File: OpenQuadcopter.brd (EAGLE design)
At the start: 100 x 100 mm, 78 parts, among them U1 MPU-6000QFN-24

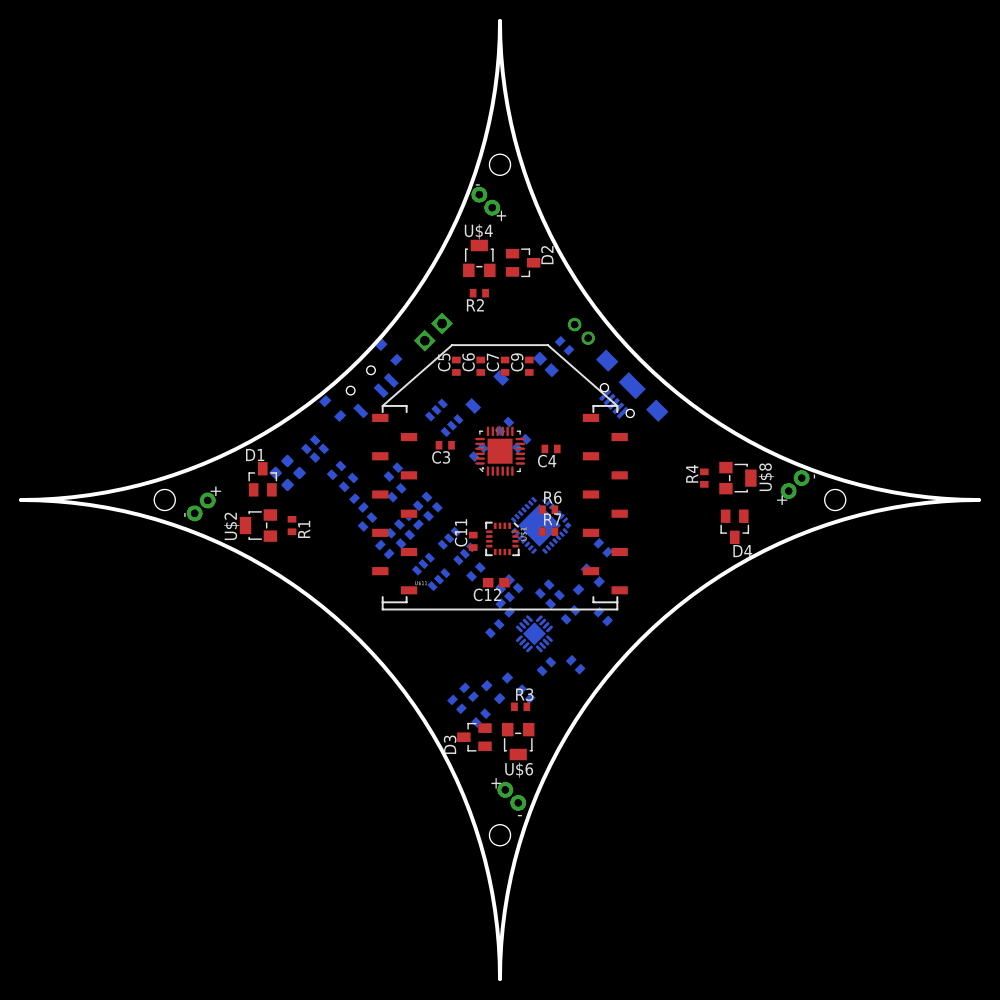
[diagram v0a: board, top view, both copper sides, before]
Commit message: smooth the corner of quadcopter.
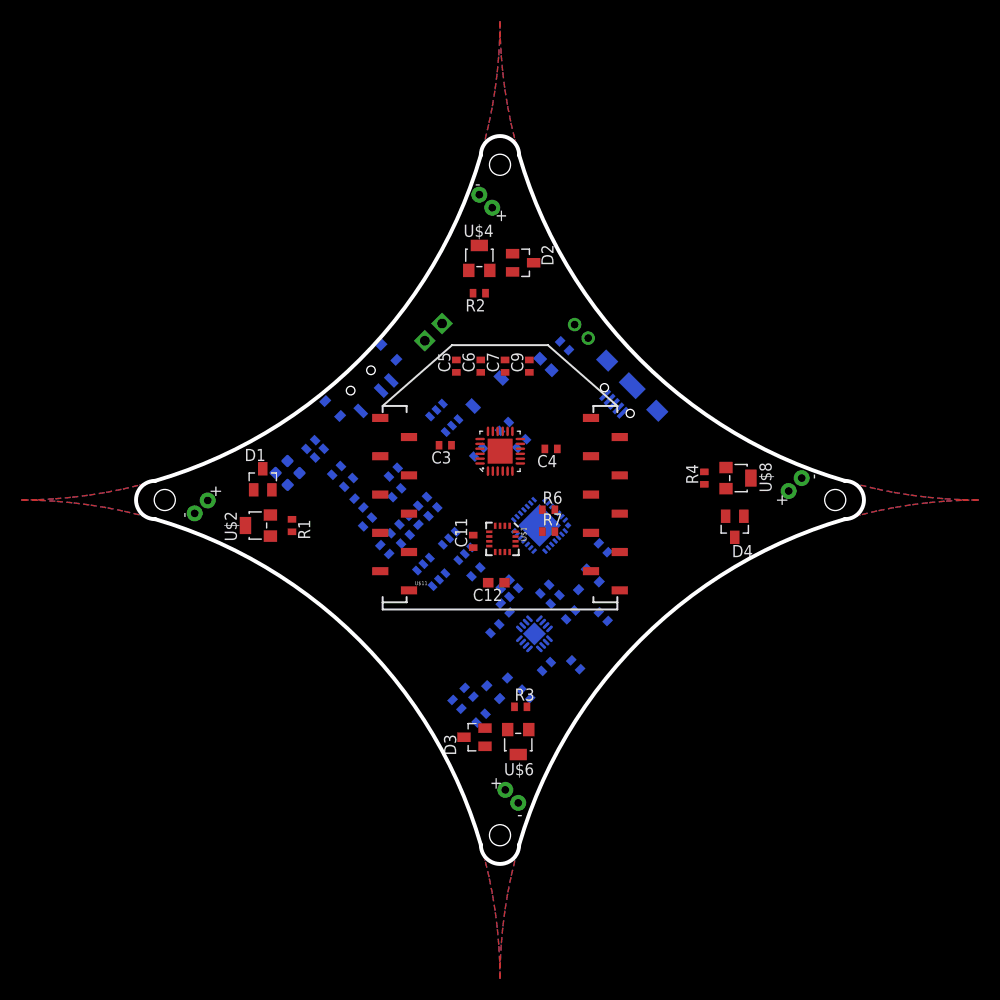
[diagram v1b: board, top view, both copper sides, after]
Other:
- board size 100 x 100 mm -> 76 x 76 mm

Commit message: Publish openquadcopter extention board.
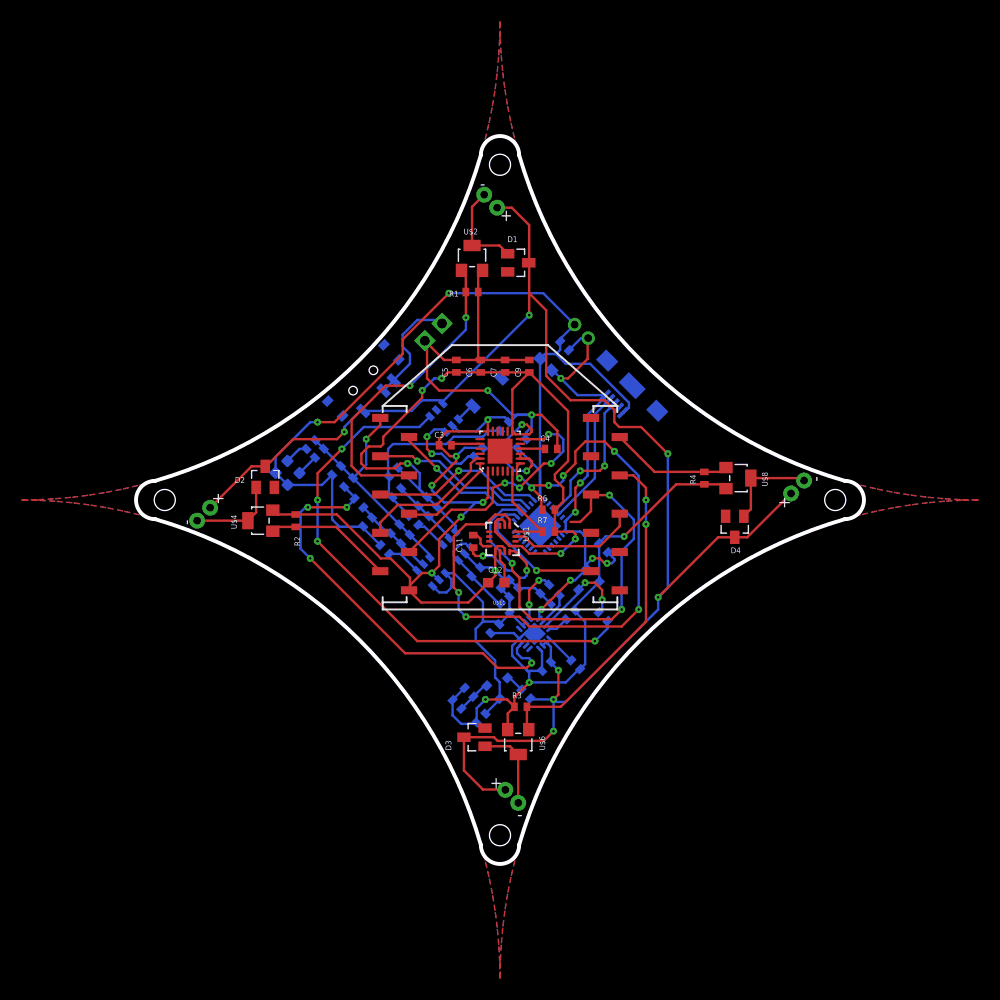
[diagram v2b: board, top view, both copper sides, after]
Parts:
- moved U$3 49.0 mm to (4.70, 34.4), turned to 0 degrees
- moved U$5 48.8 mm to (-34.2, 4.19), turned to 90 degrees
- moved U$2 35.8 mm to (-2.92, 25.3), turned to 0 degrees
- moved U$4 35.7 mm to (-25.0, -2.16), turned to 90 degrees
- moved D2 35.0 mm to (-24.5, 2.41), turned to 0 degrees
- moved D1 35.0 mm to (1.91, 24.8), turned to 270 degrees
- moved R1 30.8 mm to (-2.92, 21.7), turned to 180 degrees
- moved R2 30.5 mm to (-21.3, -2.16), turned to 270 degrees
- moved U$9 0.36 mm to (34.3, -4.32)
- moved U$12 0.25 mm to (-14.3, 12.5)
- moved U$14 0.09 mm to (4.18, -2.73), turned to 315 degrees
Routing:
- net GND: track 0.00 -> 210.9 mm, vias 0 -> 12
- net BAT: track 0.00 -> 164.2 mm, vias 0 -> 7
- net VCCA: track 0.00 -> 97.7 mm, vias 0 -> 7
- net DGND: track 0.00 -> 97.5 mm, vias 0 -> 2
- net N$4: track 0.00 -> 71.7 mm, vias 0 -> 8
- net N$15: track 0.00 -> 57.2 mm, vias 0 -> 4
- net VBUS: track 0.00 -> 49.4 mm, vias 0 -> 7
- net BOOT0: track 0.00 -> 45.5 mm, vias 0 -> 3
- net /PGOOD: track 0.00 -> 44.8 mm, vias 0 -> 4
- net MOTOR/PA6: track 0.00 -> 35.8 mm, vias 0 -> 2
- net MOTOR/PC8: track 0.00 -> 33.4 mm, vias 0 -> 2
- net VCOM: track 0.00 -> 31.8 mm
- net INT/PA4: track 0.00 -> 27.8 mm, vias 0 -> 4
- net VCCD: track 0.00 -> 24.7 mm, vias 0 -> 1
- net AGND: track 0.00 -> 20.4 mm
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
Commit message: Fixed.
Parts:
- C10, C18, C22, C23: value (none) -> 100nF
- C13, C14, C16, C21: value (none) -> 4.7uF; device openmotestm:C0402 -> openmotestm:C0603
- C15, C20: value (none) -> 15pF
- C17, C19: value (none) -> 10nF
- C24: value (none) -> 1uF
- C8: value (none) -> 10uF; device openmotestm:C0402 -> openmotestm:C0603
- R1, R11, R2, R21, R22, R24, R25, R3, R4, R9: value (none) -> 10K
- R10, R8: value (none) -> 1.2K
- R12: value (none) -> 10R
- R13: value (none) -> 39K
- R14, R16: value (none) -> 30K
- R15: value (none) -> 42.2K
- R17: value (none) -> 150K
- R18: value (none) -> 300K
- R19, R20: value (none) -> 1K
- R23: value (none) -> 100K
- R26: value (none) -> 20K
- R27, R28: value (none) -> 0R
- U$1: value HMC5883LSMD -> HMC5883L-SMD
- U$2, U$4, U$6, U$8: value MOSFET -> PWV31XN
- U1: value MPU-6000QFN-24 -> MPU-6050QFN-24
- moved C13 15.5 mm to (-0.37, -24.2), turned to 315 degrees
- moved C14 2.05 mm to (-0.80, -8.62)
- moved C16 1.18 mm to (-12.0, 2.11)
- moved C21 1.08 mm to (-17.9, 2.47), turned to 315 degrees
- moved C8 0.27 mm to (5.08, -17.5)
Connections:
- net DGND: now also C21.2; no longer C21.1
- net VCCD: now also C21.1; no longer C21.2
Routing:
- net GND: track 210.9 -> 223.8 mm, vias 12 -> 13
- net AGND: track 20.4 -> 21.5 mm
- net VCOM: track 31.8 -> 32.8 mm
- net DGND: track 97.5 -> 96.7 mm
- net VCCD: track 24.7 -> 25.4 mm
- net VCCA: track 97.7 -> 97.1 mm
